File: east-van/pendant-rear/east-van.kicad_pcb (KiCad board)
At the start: 2 copper layers, 49.4 x 83.3 mm, 11 parts

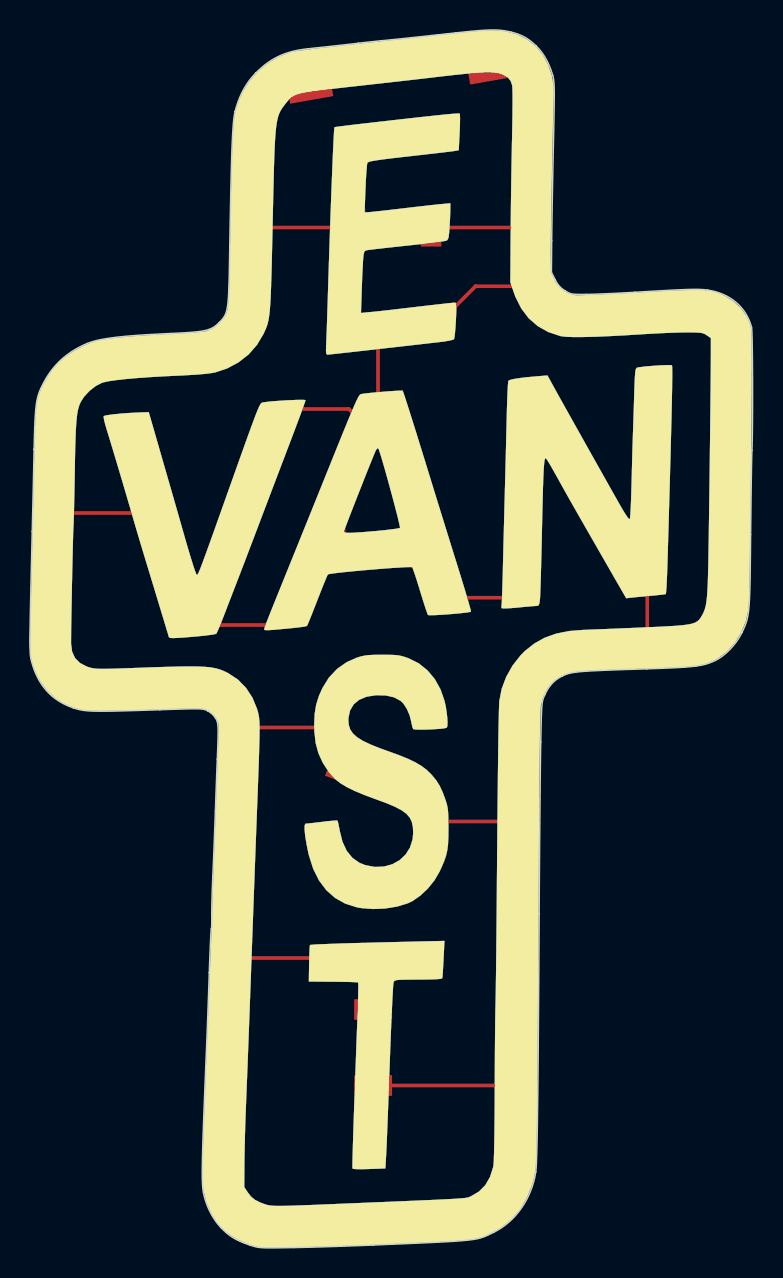
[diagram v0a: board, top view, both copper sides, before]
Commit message: east-van/pendant-rear: flip silk and mask to create rear (with mirrored writing)
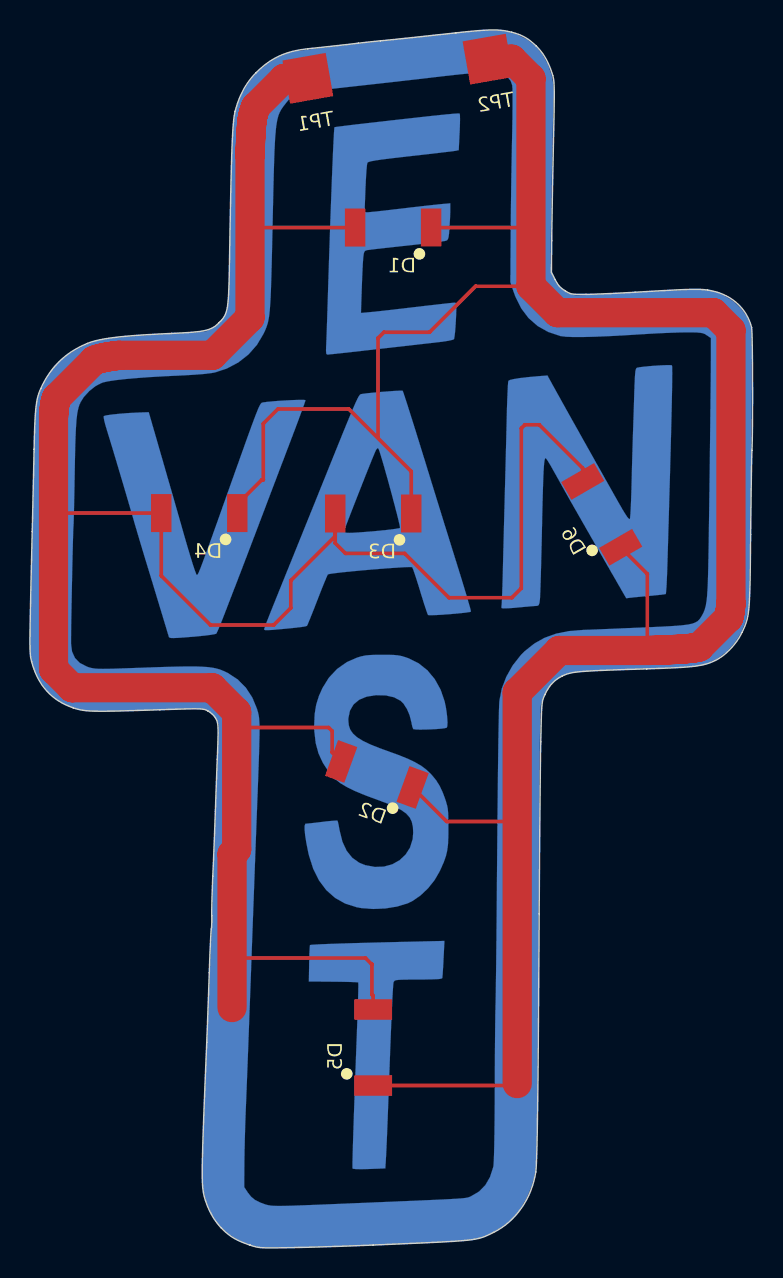
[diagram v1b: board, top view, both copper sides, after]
